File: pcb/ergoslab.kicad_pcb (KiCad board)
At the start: 2 copper layers, 114.5 x 101.2 mm, 102 parts, among them J1 L_B_LED, J2 R_B_LED, J3 SLAVE_LED, P1 OLED, P2 ICSP, SW0:0 SW_Push, SW0:1 SW_Push, SW0:2 SW_Push, SW0:3 SW_Push, SW0:4 SW_Push, SW1:0 SW_Push, SW1:1 SW_Push, SW1:2 SW_Push, SW1:3 SW_Push, SW1:4 SW_Push, SW2:0 SW_Push, SW2:1 SW_Push, SW2:2 SW_Push, SW2:3 SW_Push, SW2:4 SW_Push, SW3:0 SW_Push, SW3:1 SW_Push, SW3:2 SW_Push, SW3:3 SW_Push, SW3:4 SW_Push, SW3:5 SW_Push, SW4:1 SW_Push, SW4:2 SW_Push, SW4:3 SW_Push, SW4:4 SW_Push, SW4:5 SW_Push

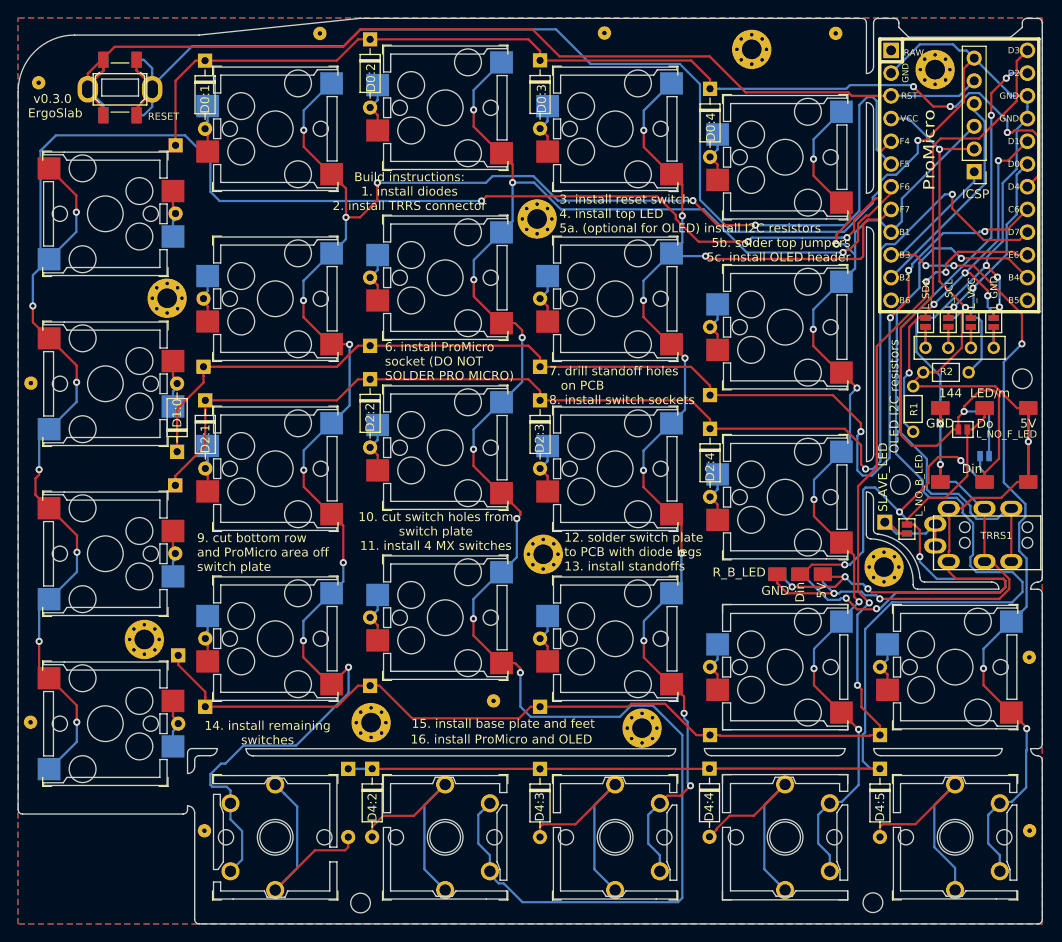
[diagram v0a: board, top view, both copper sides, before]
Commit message: fix: make all switchplate cutouts 14mm so switches will actually fit
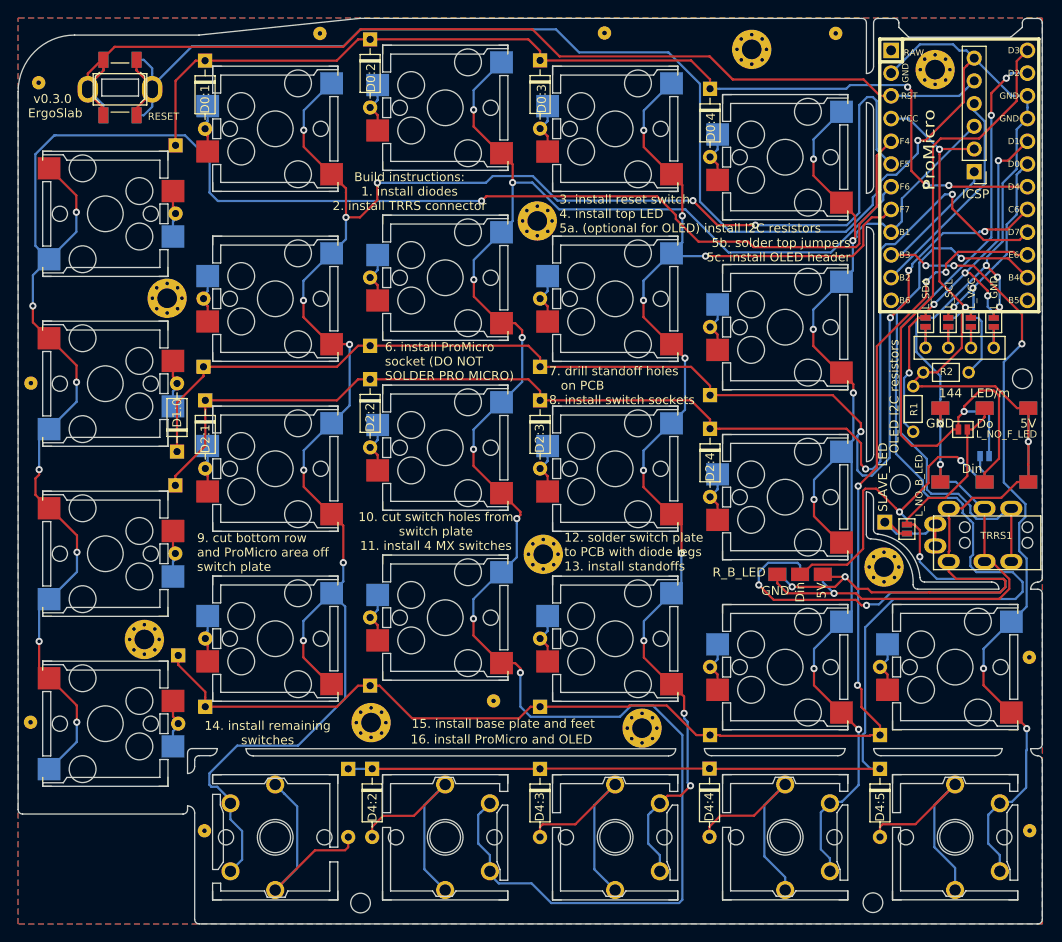
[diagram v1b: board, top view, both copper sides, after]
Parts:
- moved Drill 0.22 mm to (130.5, 66.8)
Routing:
- net Net-(J1-Pad2): track 60.2 -> 71.6 mm
- net Col1: track 206.8 -> 212.8 mm, vias 11 -> 10
- net Col4: track 130.1 -> 135.6 mm, vias 8 -> 7
- net Col0: track 205.6 -> 209.0 mm, vias 10 -> 8
- net Row0: track 120.0 -> 118.1 mm
- net Row3: track 156.4 -> 155.3 mm
- net Col3: track 135.1 -> 134.0 mm
- net Col2: track 211.5 -> 210.5 mm, vias 9 -> 8
- net Net-(D4:4-Pad2): track 24.6 -> 25.3 mm
- net Net-(J2-Pad2): track 39.4 -> 39.1 mm, vias 3 -> 2
- net GND: track 267.6 -> 267.7 mm, vias 8 -> 7
- net VCC: vias 6 -> 5
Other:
- outline, holes or cut-outs redrawn

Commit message: chore: add refs for switchplate supports
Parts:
- renumbered REF** to BRACE0, REF** to BRACE1, REF** to BRACE2, REF** to BRACE3, REF** to BRACE4, REF** to BRACE5, REF** to BRACE6, REF** to BRACE7, REF** to BRACE8, REF** to BRACE9
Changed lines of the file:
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@@
   (module footprints:switchplate-brace (layer F.Cu)
     (at 185.53 135.01)
-    (fp_text reference REF** (at 0.4 1.4) (layer F.SilkS) hide
+    (fp_text reference BRACE7 (at 0.4 1.4) (layer F.SilkS) hide
       (effects (font (size 1 1) (thickness 0.15)))
     )
@@
   (module footprints:switchplate-brace (layer F.Cu)
     (at 93.28 135.02)
-    (fp_text reference REF** (at 0.4 1.4) (layer F.SilkS) hide
+    (fp_text reference BRACE8 (at 0.4 1.4) (layer F.SilkS) hide
       (effects (font (size 1 1) (thickness 0.15)))
     )
@@
   (module footprints:switchplate-brace (layer F.Cu)
     (at 125.6 120.5)
-    (fp_text reference REF** (at 0.4 1.4) (layer F.SilkS) hide
+    (fp_text reference BRACE9 (at 0.4 1.4) (layer F.SilkS) hide
       (effects (font (size 1 1) (thickness 0.15)))
     )
@@
   (module footprints:switchplate-brace (layer F.Cu)
     (at 185.49 115.63)
-    (fp_text reference REF** (at 0.4 1.4) (layer F.SilkS) hide
+    (fp_text reference BRACE6 (at 0.4 1.4) (layer F.SilkS) hide
       (effects (font (size 1 1) (thickness 0.15)))
     )
@@
   (module footprints:switchplate-brace (layer F.Cu)
     (at 163.85 45.88)
-    (fp_text reference REF** (at 0.4 1.4) (layer F.SilkS) hide
+    (fp_text reference BRACE5 (at 0.4 1.4) (layer F.SilkS) hide
       (effects (font (size 1 1) (thickness 0.15)))
     )
@@
   (module footprints:switchplate-brace (layer F.Cu)
     (at 138 45.84)
-    (fp_text reference REF** (at 0.4 1.4) (layer F.SilkS) hide
+    (fp_text reference BRACE4 (at 0.4 1.4) (layer F.SilkS) hide
       (effects (font (size 1 1) (thickness 0.15)))
     )
@@
   (module footprints:switchplate-brace (layer F.Cu)
     (at 106.19 45.89)
-    (fp_text reference REF** (at 0.4 1.4) (layer F.SilkS) hide
+    (fp_text reference BRACE3 (at 0.4 1.4) (layer F.SilkS) hide
       (effects (font (size 1 1) (thickness 0.15)))
     )
@@
   (module footprints:switchplate-brace (layer F.Cu)
     (at 74.75 51.4)
-    (fp_text reference REF** (at 0.4 1.4) (layer F.SilkS) hide
+    (fp_text reference BRACE2 (at 0.4 1.4) (layer F.SilkS) hide
       (effects (font (size 1 1) (thickness 0.15)))
     )
@@
   (module footprints:switchplate-brace (layer F.Cu)
     (at 73.88 84.98)
-    (fp_text reference REF** (at 0.4 1.4) (layer F.SilkS) hide
+    (fp_text reference BRACE1 (at 0.4 1.4) (layer F.SilkS) hide
       (effects (font (size 1 1) (thickness 0.15)))
     )
@@
   (module footprints:switchplate-brace (layer F.Cu)
     (at 73.84 122.89)
-    (fp_text reference REF** (at 0.4 1.4) (layer F.SilkS) hide
+    (fp_text reference BRACE0 (at 0.4 1.4) (layer F.SilkS) hide
       (effects (font (size 1 1) (thickness 0.15)))
     )
